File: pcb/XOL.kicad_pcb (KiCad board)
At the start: 2 copper layers, 77.5 x 50.8 mm, 70 parts, among them J1 Conn_01x10_Socket, J10 Conn_01x02_Socket, J11 Conn_01x02_Socket, J12 Conn_01x02_Socket, J13 Conn_01x02_Socket, J14 Conn_01x02_Socket, J15 Conn_01x02_Socket, J16 Conn_01x02_Socket, J17 Conn_01x02_Socket, J18 Conn_01x02_Socket, J19 Conn_01x02_Socket, J2 Conn_01x02_Pin, J20 Conn_01x02_Socket, J21 Conn_01x02_Socket, J22 Conn_01x02_Socket, J23 Conn_01x02_Socket, J24 Conn_01x02_Socket, J25 Conn_01x02_Socket, J26 Conn_01x02_Socket, J27 Conn_01x02_Socket, J28 Conn_01x02_Socket, J29 Conn_01x02_Socket, J3 Conn_01x10_Socket, J30 Conn_01x02_Socket, J31 Conn_01x02_Socket, J32 Conn_01x02_Socket, J33 Conn_01x02_Socket, J4 Conn_02x02_Counter_Clockwise, J5 Conn_02x02_Counter_Clockwise, J6 Conn_02x02_Counter_Clockwise, J7 Conn_02x02_Counter_Clockwise, J8 Conn_02x02_Counter_Clockwise, J9 Conn_02x02_Counter_Clockwise, U1 4070, U2 4070

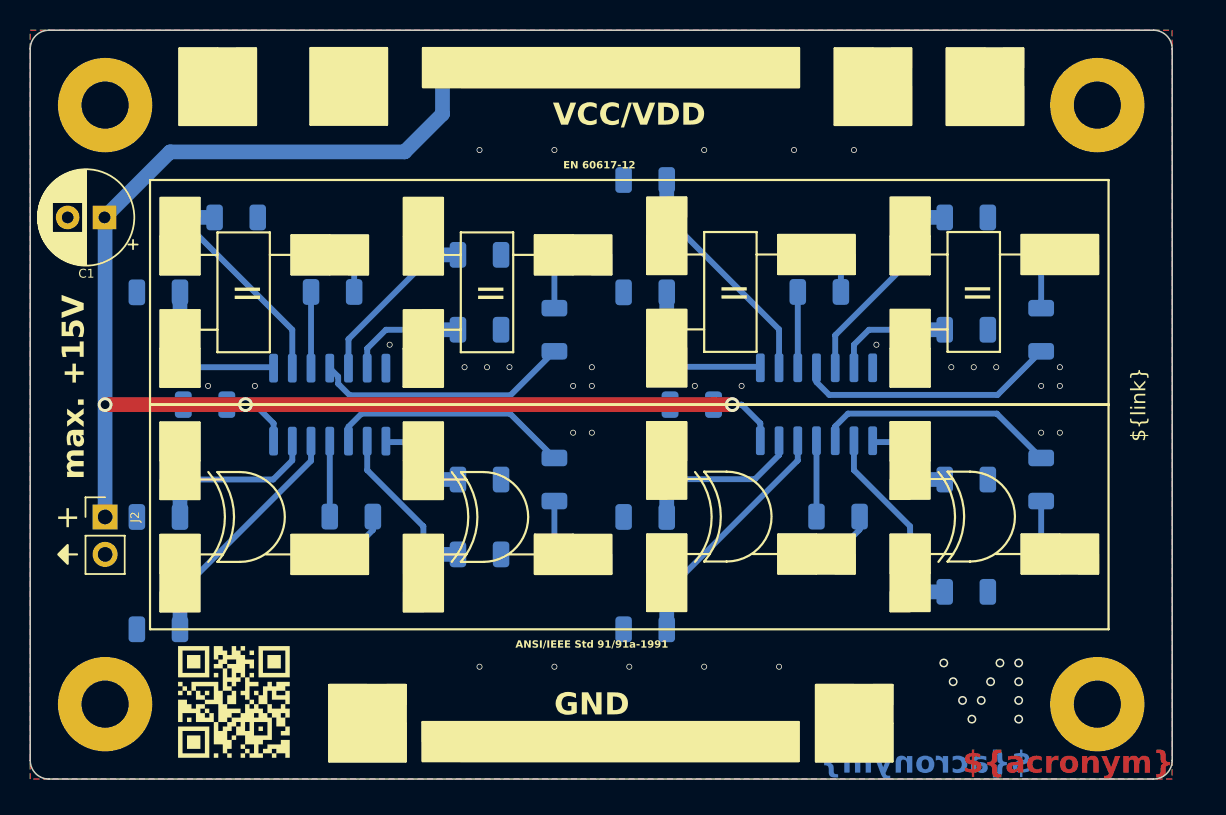
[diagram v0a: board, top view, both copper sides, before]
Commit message: Add reverse polarity protection
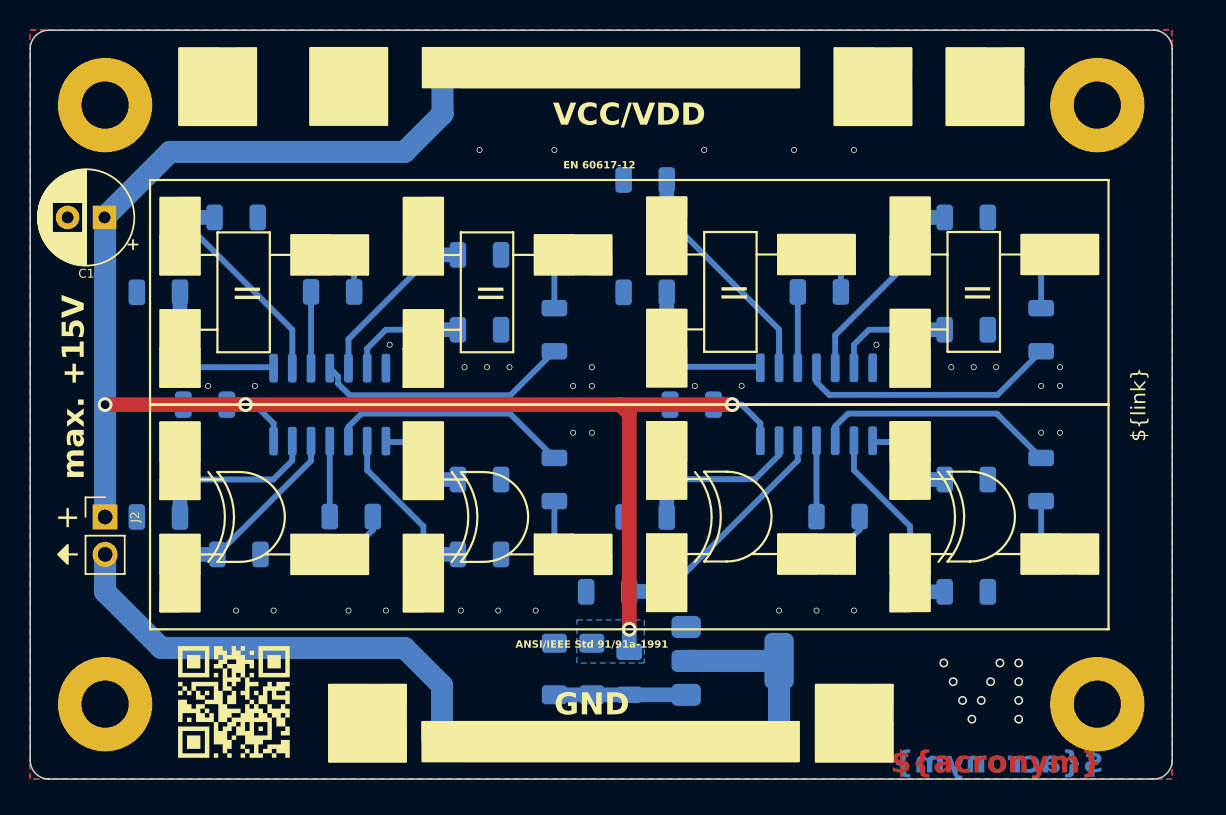
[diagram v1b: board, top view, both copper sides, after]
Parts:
- added D1: BAT43, Diode_SMD:D_MiniMELF, B.Cu at (157.5, 119.5)
- added D2: BZ5V1, Diode_SMD:D_MiniMELF, B.Cu at (154.9, 119.5)
- added Q1: BUK7880-55A, Package_TO_SOT_SMD:SOT-223-3_TabPin2, B.Cu at (167.0, 119.0)
- added R25: 1k, Resistor_SMD:R_1206_3216Metric, B.Cu at (160.0, 119.8)
- moved FID1 37.8 mm to (149.9, 84.5)
- moved FID3 36.9 mm to (168.3, 84.5)
- moved FID2 35.5 mm to (156.2, 84.5)
- moved R16 7.46 mm to (133.5, 111.8), turned to 180 degrees
- moved R24 3.59 mm to (158.6, 114.3)
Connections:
- J2 pad 2: GND -> Net-(J2-Pin_2)
- J3 pad 1: GND -> Net-(J2-Pin_2)
- J3 pad 10: GND -> Net-(J2-Pin_2)
- J3 pad 2: GND -> Net-(J2-Pin_2)
- J3 pad 3: GND -> Net-(J2-Pin_2)
- J3 pad 4: GND -> Net-(J2-Pin_2)
- J3 pad 5: GND -> Net-(J2-Pin_2)
- J3 pad 6: GND -> Net-(J2-Pin_2)
- J3 pad 7: GND -> Net-(J2-Pin_2)
- J3 pad 8: GND -> Net-(J2-Pin_2)
- J3 pad 9: GND -> Net-(J2-Pin_2)
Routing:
- net Net-(J2-Pin_2): track 0.00 -> 43.6 mm
- net VCC: track 101.6 -> 118.6 mm, vias 3 -> 4
- net Net-(D1-A): track 0.00 -> 8.94 mm
- net Net-(J17-Pin_1): track 19.0 -> 15.4 mm
- net GND: vias 43 -> 48
- added copper zone on B.Cu, net Net-(J2-Pin_2)
